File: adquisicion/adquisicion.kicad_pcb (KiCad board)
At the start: 2 copper layers, 125.6 x 103.2 mm, 34 parts, among them J1 Coax Antena 1, J2 Coax Antena 2, J3 Screw_Terminal_01x04, J5 Conn_01x08_Socket, J6 Conn_01x15_Pin, J7 Conn_01x10_Socket, U2 L7805, U3 YAAJ_BluePill_Part_Like

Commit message: Mejoras layout, corrección ERC y DRC
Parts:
- added R7: 0, huellas_proyecto:R_Axial_DIN0207_L6.3mm_D2.5mm_P15.24mm_Horizontal-pad2mm, F.Cu at (165.5, 150.6)
- ICSP1: footprint Connector_PinHeader_2.54mm:PinHeader_2x03_P2.54mm_Vertical -> huellas_proyecto:PinHeader_2x03_P2.54mm_Vertical-pad2mm
- J5: footprint Connector_PinHeader_2.54mm:PinHeader_1x08_P2.54mm_Vertical -> huellas_proyecto:PinHeader_1x08_P2.54mm_Vertical-pad2mm
- J6: footprint Connector_PinHeader_2.54mm:PinHeader_1x15_P2.54mm_Vertical -> huellas_proyecto:PinHeader_1x15_P2.54mm_Vertical-pad2mm
- J7: footprint Connector_PinHeader_2.54mm:PinHeader_1x10_P2.54mm_Vertical -> huellas_proyecto:PinHeader_1x10_P2.54mm_Vertical-2mm
- U3: footprint Footprints:YAAJ_BluePill_2 -> huellas_proyecto:YAAJ_BluePill_2
- moved D7 43.6 mm to (198.7, 77.4), turned to -90 degrees
- moved D8 34.5 mm to (190.6, 77.4), turned to -90 degrees
- moved D1 34.0 mm to (210.9, 83.6), turned to 90 degrees
- moved C5 32.8 mm to (168.5, 78.0), turned to -90 degrees
- moved J3 28.0 mm to (207.5, 61.9)
- moved D2 26.2 mm to (202.8, 83.6), turned to 90 degrees
- moved D3 24.5 mm to (194.6, 83.6), turned to 90 degrees
- moved D5 24.3 mm to (215.0, 77.4), turned to -90 degrees
- moved D6 18.9 mm to (206.9, 77.4), turned to -90 degrees
- moved D4 15.8 mm to (186.5, 83.6), turned to 90 degrees
- moved U2 11.3 mm to (157.5, 78.0), turned to 0 degrees
- moved C4 10.6 mm to (150.5, 78.0), turned to -90 degrees
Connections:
- U3 pad 37: Reset -> Net-(U3-RST)
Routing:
- net +5V: track 6.18 -> 77.1 mm
- net Reset: track 97.6 -> 33.0 mm
- net GND: track 73.8 -> 132.6 mm, vias 11 -> 47
- net Net-(U3-RST): track 0.00 -> 31.9 mm
- net +3V3: track 14.2 -> 43.3 mm
- net Net-(D2-A): track 25.7 -> 17.4 mm
- net +24V: track 133.8 -> 141.5 mm
- net Net-(D3-A): track 25.4 -> 18.4 mm
- net Net-(D4-A): track 17.7 -> 20.4 mm
- net SCK: track 38.7 -> 41.4 mm
- net MISO: track 28.9 -> 30.8 mm
- net MOSI: track 28.8 -> 29.9 mm
- net Net-(D1-A): track 18.0 -> 18.7 mm
- removed copper zone on B.Cu, net +24V
- removed copper zone on B.Cu, net +3V3
- removed copper zone on B.Cu, net +5V
- removed copper zone on B.Cu, net 5v-pour

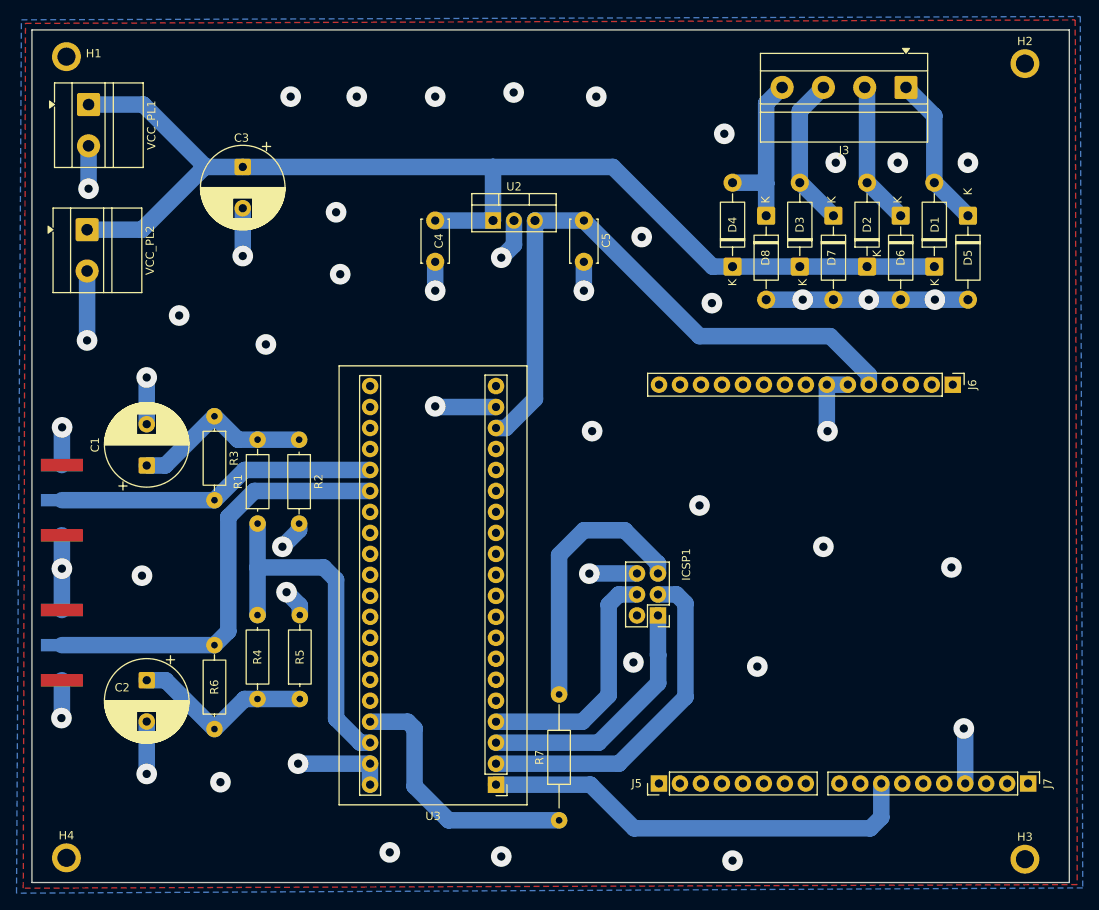
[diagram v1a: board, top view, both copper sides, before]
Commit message: Modificación posición C5 C6 en placa Acondicionador y cambio de huella sma (verificar), cambio de huella sma en placa Adquisición (verificar)
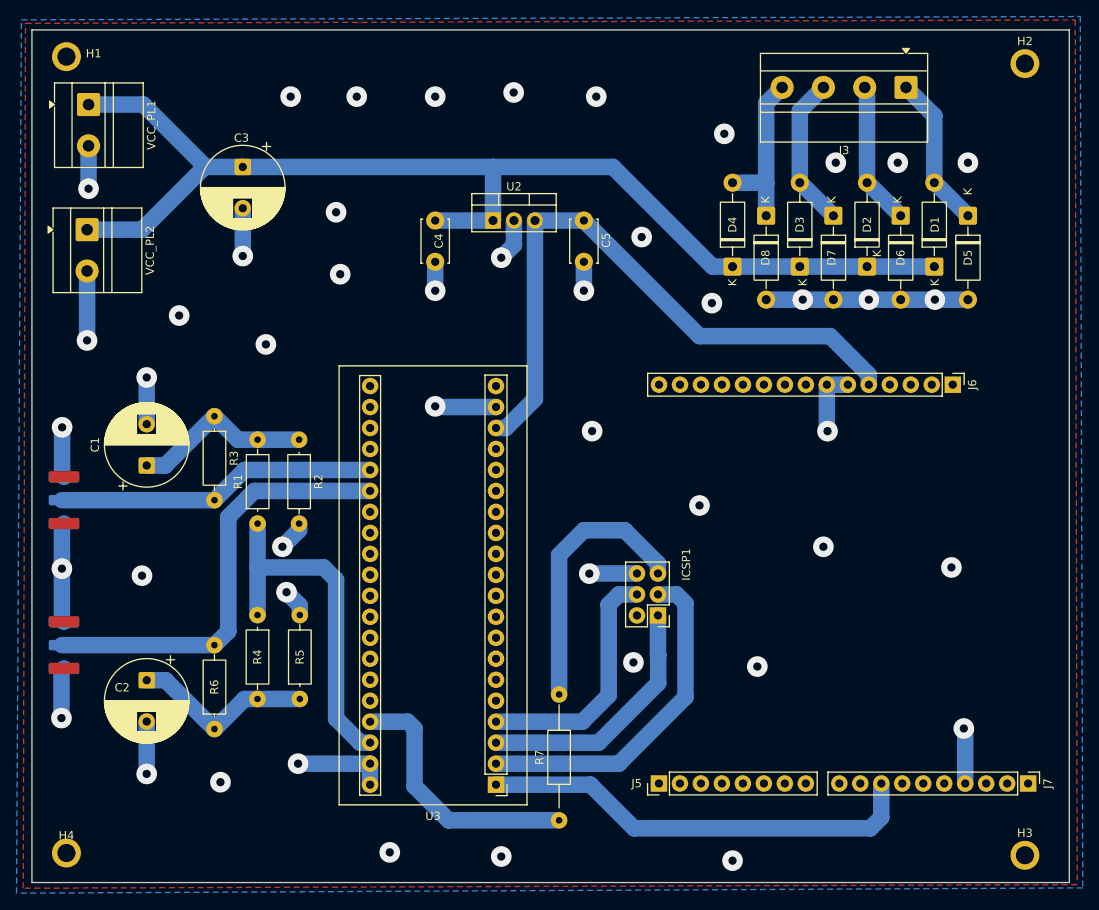
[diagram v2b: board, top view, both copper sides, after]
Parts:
- J1, J2: footprint Connector_Coaxial:SMA_Amphenol_132289_EdgeMount -> Connector_Coaxial:SMA_Samtec_SMA-J-P-H-ST-EM1_EdgeMount
- moved H3 0.47 mm to (221.9, 154.8)
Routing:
- net GND: track 132.6 -> 138.8 mm
